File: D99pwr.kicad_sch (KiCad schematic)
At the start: 41 parts, among them IC1 TPS560430YFQDBVRQ1, IC2 NCP730BMT1500TBG, Q3 BC847BDW1, U2 MAX40203AUK, U3 MCP1640BCH, U4 MAX40203AUK

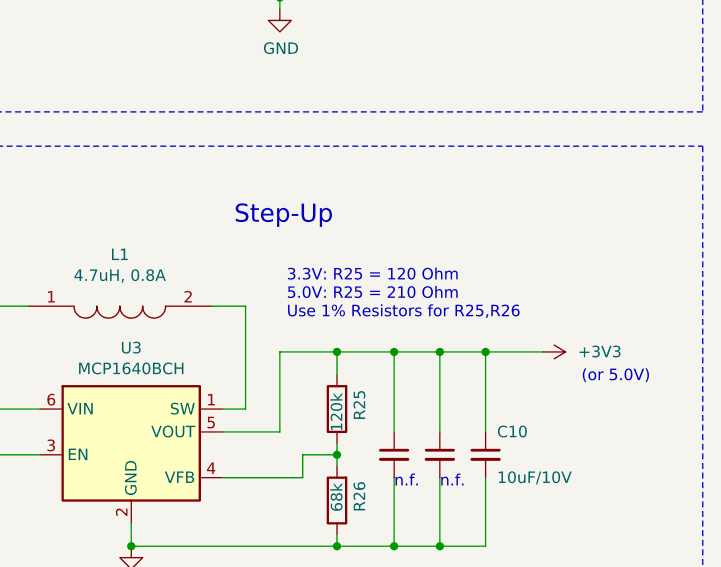
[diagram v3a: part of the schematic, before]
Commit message: fix: R25 had incorrect footnote
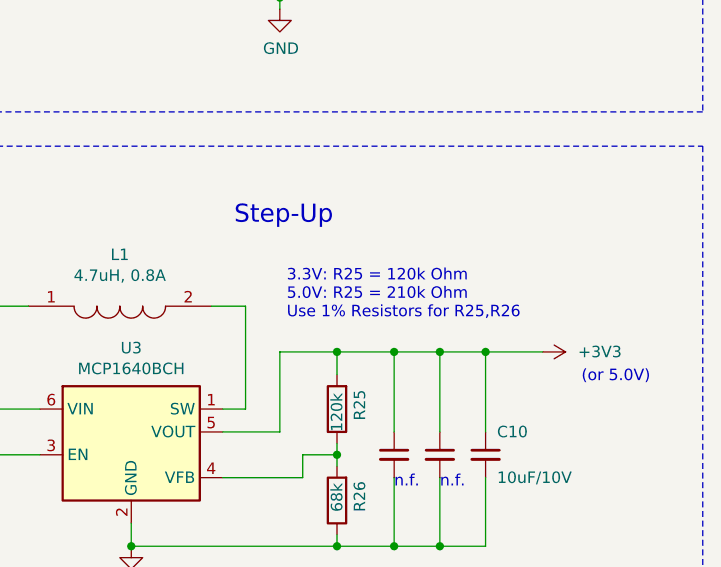
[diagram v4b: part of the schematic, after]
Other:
- note added: "3.3V: R25 = 120k Ohm 5.0V: R25 = 210k Ohm Use 1% Resistors for R25,R26"
- note removed: "3.3V: R25 = 120 Ohm 5.0V: R25 = 210 Ohm Use 1% Resistors for R25,R26"
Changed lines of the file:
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@@
 	(title_block
 		(title "DCC Ambient Decoder Prototype")
-		(date "2025-10-14")
-		(rev "1")
+		(date "2026-01-19")
+		(rev "1.1")
 		(company "Frank Schumacher")
 		(comment 1 "D99.1")
@@
 		)
 	)
-	(text "3.3V: R25 = 120 Ohm\n5.0V: R25 = 210 Ohm\nUse 1% Resistors for R25,R26"
+	(text "3.3V: R25 = 120k Ohm\n5.0V: R25 = 210k Ohm\nUse 1% Resistors for R25,R26"
 		(exclude_from_sim no)
 		(at 228.092 95.25 0)
